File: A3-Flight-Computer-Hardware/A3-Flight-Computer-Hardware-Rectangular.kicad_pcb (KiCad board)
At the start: 4 copper layers, 70 x 40 mm, 68 parts, among them J1 BAT, J2 ST1W008S4ER1500, J3 USB_C_Receptacle_USB2.0_14P, J4 Debug Header, J5 Cam 1, J6 Cam 2, J8 Telem, J9 CAN, Q1 IRLML0030, SW1 BOOT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

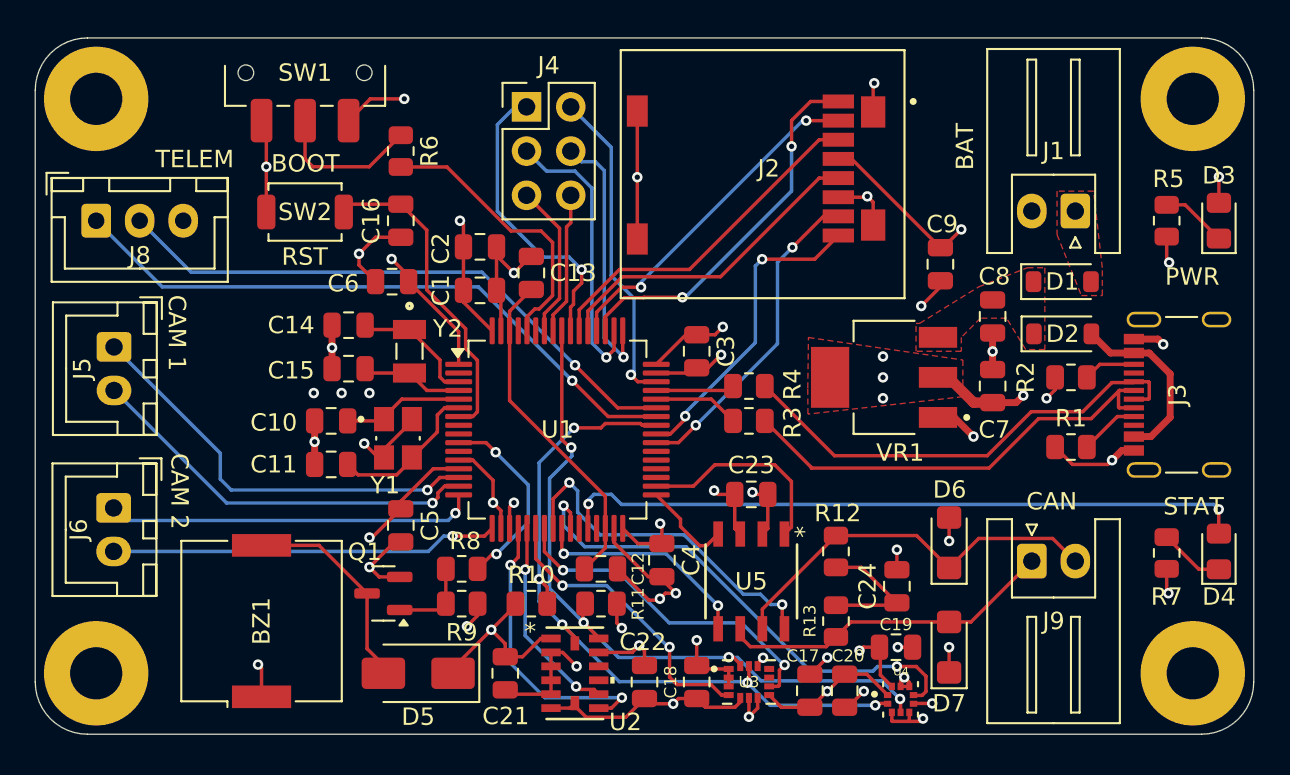
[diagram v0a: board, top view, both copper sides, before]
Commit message: Small routing changes
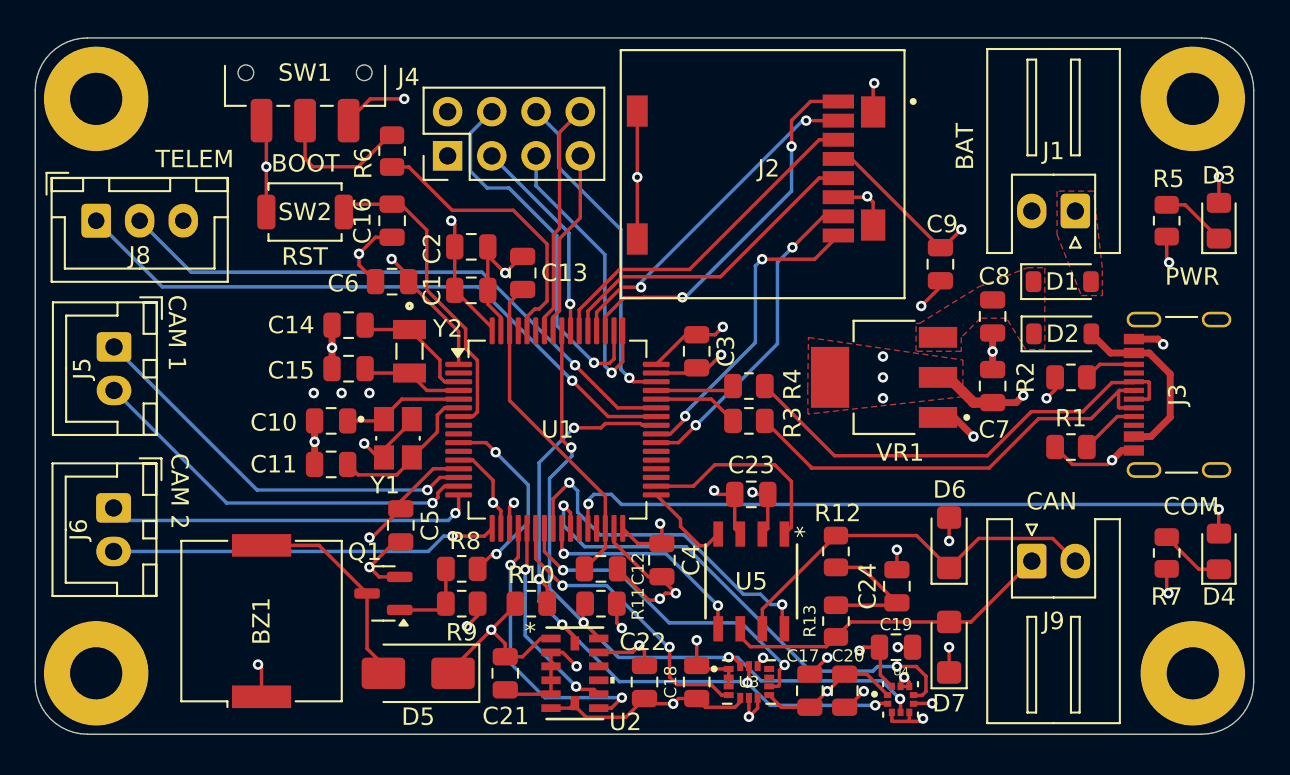
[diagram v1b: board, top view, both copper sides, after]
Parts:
- J4: value Debug Header -> Conn_02x04_Odd_Even; footprint Connector_PinHeader_2.54mm:PinHeader_2x03_P2.54mm_Vertical -> Connector_PinHeader_2.54mm:PinHeader_2x04_P2.54mm_Vertical
- moved J4 5.34 mm to (138.2, 88.3), turned to 90 degrees
- moved C1 0.50 mm to (139.6, 96.0)
- moved C13 0.50 mm to (142.5, 95.0)
- moved C16 0.50 mm to (135.0, 92.0)
- moved C2 0.50 mm to (139.6, 93.5)
- moved R6 0.50 mm to (135.0, 88.0)
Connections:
- J4 pad 1: /JTDO-SWO -> GND
- J4 pad 2: /JTMS-SWDIO -> +3.3V
- J4 pad 3: /JTDI -> /JTDO-SWO
- J4 pad 4: /JTCK-SWCLK -> /JTDI
- J4 pad 5: /DEBUG_RX -> /JTCK-SWCLK
- J4 pad 6: /DEBUG_TX -> /JTMS-SWDIO
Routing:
- net /JTDO-SWO: track 17.1 -> 11.9 mm
- net /JTDI: track 16.4 -> 21.5 mm
- net /DEBUG_RX: track 8.93 -> 13.4 mm
- net /DEBUG_TX: track 8.21 -> 10.7 mm
- net /JTCK-SWCLK: track 15.1 -> 16.9 mm
- net /CAM1_TX: track 24.4 -> 23.5 mm
- net /JTMS-SWDIO: track 18.6 -> 19.2 mm
- net /BOOT: track 16.3 -> 15.8 mm
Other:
- board text added: "COM"
- board text removed: "STAT"

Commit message: Added labels and changed component sizes
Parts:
- removed the D5 at (136.5, 118.0)
- added C7: 100nF, Capacitor_SMD:C_0402_1005Metric, F.Cu at (141.2, 111.2)
- added D4: LED, LED_SMD:LED_0805_2012Metric_Pad1.15x1.40mm_HandSolder, F.Cu at (179.0, 111.0)
- added D6: DSS14U, Diode_SMD:D_SOD-123, F.Cu at (134.5, 116.0)
- added R7: 240R, Resistor_SMD:R_0402_1005Metric, F.Cu at (179.0, 108.0)
- added TP3: SDA, TestPoint:TestPoint_THTPad_1.0x1.0mm_Drill0.5mm, F.Cu at (165.9, 118.0)
- added TP4: SCL, TestPoint:TestPoint_THTPad_1.0x1.0mm_Drill0.5mm, F.Cu at (162.9, 118.0)
- C10: renamed from C9; footprint Capacitor_SMD:C_0805_2012Metric -> Capacitor_SMD:C_0402_1005Metric
- C11: renamed from C10; footprint Capacitor_SMD:C_0805_2012Metric -> Capacitor_SMD:C_0402_1005Metric
- C12: renamed from C11; footprint Capacitor_SMD:C_0805_2012Metric -> Capacitor_SMD:C_0402_1005Metric
- C13: renamed from C12; footprint Capacitor_SMD:C_0805_2012Metric -> Capacitor_SMD:C_0402_1005Metric
- C14: renamed from C13; footprint Capacitor_SMD:C_0805_2012Metric -> Capacitor_SMD:C_0402_1005Metric
- C15: renamed from C14; footprint Capacitor_SMD:C_0805_2012Metric -> Capacitor_SMD:C_0402_1005Metric
- C16: renamed from C15; footprint Capacitor_SMD:C_0805_2012Metric -> Capacitor_SMD:C_0402_1005Metric
- C17: renamed from C16; footprint Capacitor_SMD:C_0805_2012Metric -> Capacitor_SMD:C_0402_1005Metric
- C18: renamed from C17; footprint Capacitor_SMD:C_0805_2012Metric -> Capacitor_SMD:C_0402_1005Metric
- C19: renamed from C18; footprint Capacitor_SMD:C_0805_2012Metric -> Capacitor_SMD:C_0402_1005Metric
- C2, C3, C4, C5, C6: footprint Capacitor_SMD:C_0805_2012Metric -> Capacitor_SMD:C_0402_1005Metric
- C20: renamed from C19; footprint Capacitor_SMD:C_0805_2012Metric -> Capacitor_SMD:C_0402_1005Metric
- C21: renamed from C20; footprint Capacitor_SMD:C_0805_2012Metric -> Capacitor_SMD:C_0402_1005Metric
- C22: renamed from C21; footprint Capacitor_SMD:C_0805_2012Metric -> Capacitor_SMD:C_0402_1005Metric
- C23: renamed from C22; footprint Capacitor_SMD:C_0805_2012Metric -> Capacitor_SMD:C_0402_1005Metric
- C24: renamed from C23; footprint Capacitor_SMD:C_0805_2012Metric -> Capacitor_SMD:C_0402_1005Metric
- C25: renamed from C24; footprint Capacitor_SMD:C_0805_2012Metric -> Capacitor_SMD:C_0402_1005Metric
- J4: renamed from J5; footprint Connector_JST:JST_XH_B2B-XH-A_1x02_P2.50mm_Vertical -> Connector_JST:JST_XH_S2B-XH-A_1x02_P2.50mm_Horizontal
- J5: renamed from J4; value Conn_02x04_Odd_Even -> DEBUG
- J6: footprint Connector_JST:JST_XH_B2B-XH-A_1x02_P2.50mm_Vertical -> Connector_JST:JST_XH_S2B-XH-A_1x02_P2.50mm_Horizontal
- J7: renamed from J8; footprint Connector_JST:JST_XH_B3B-XH-A_1x03_P2.50mm_Vertical -> Connector_JST:JST_XH_S3B-XH-A_1x03_P2.50mm_Horizontal
- R1, R2, R3, R4, R5, R6: footprint Resistor_SMD:R_0805_2012Metric -> Resistor_SMD:R_0402_1005Metric
- R10: renamed from R9; footprint Resistor_SMD:R_0805_2012Metric -> Resistor_SMD:R_0402_1005Metric
- R11: renamed from R10; footprint Resistor_SMD:R_0805_2012Metric -> Resistor_SMD:R_0402_1005Metric
- R12: renamed from R11; footprint Resistor_SMD:R_0805_2012Metric -> Resistor_SMD:R_0402_1005Metric
- R13: renamed from R12; footprint Resistor_SMD:R_0805_2012Metric -> Resistor_SMD:R_0402_1005Metric
- R14: renamed from R13; footprint Resistor_SMD:R_0805_2012Metric -> Resistor_SMD:R_0402_1005Metric
- R8: renamed from R7; footprint Resistor_SMD:R_0805_2012Metric -> Resistor_SMD:R_0402_1005Metric
- R9: renamed from R8; footprint Resistor_SMD:R_0805_2012Metric -> Resistor_SMD:R_0402_1005Metric
- moved J7 20.6 mm to (124.5, 111.6)
- moved C22 17.5 mm to (159.0, 117.0)
- moved BZ1 14.1 mm to (141.5, 116.5), turned to 180 degrees
- moved C19 12.3 mm to (163.5, 113.0), turned to -90 degrees
- moved U4 11.0 mm to (155.0, 113.5), turned to -90 degrees
- moved U2 10.0 mm to (155.5, 118.0), turned to -90 degrees
- moved C21 9.60 mm to (155.0, 111.5), turned to 180 degrees
- moved J4 8.46 mm to (124.4, 92.8)
- moved J6 8.29 mm to (124.4, 102.2)
- moved R11 8.25 mm to (151.0, 112.0), turned to -90 degrees
- moved C20 7.58 mm to (157.0, 113.5), turned to -90 degrees
- moved U3 6.87 mm to (161.1, 114.5), turned to 90 degrees
- moved D8 6.58 mm to (166.0, 110.0), turned to 0 degrees
- moved C18 6.02 mm to (163.5, 115.0)
- moved R14 5.63 mm to (161.7, 109.5)
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- renumbered C7 to C8, C8 to C9, D4 to D5, D6 to D7, D7 to D8, J9 to J8
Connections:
- net /STAT_LED renamed /STAT_LED2
- U1 pad 10: /BUZZ -> unconnected-(U1-PC2-Pad10)
- U1 pad 24: /CAN_STBD -> /BUZZ
- U1 pad 25: /CAN_SHD -> unconnected-(U1-PC5-Pad25)
- U1 pad 27: unconnected-(U1-PB1-Pad27) -> /STAT_LED1
- U1 pad 35: unconnected-(U1-PB14-Pad35) -> /CAN_SHD
- U1 pad 36: unconnected-(U1-PB15-Pad36) -> /CAN_STBD
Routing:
- net +3.3V: track 96.3 -> 50.7 mm, vias 22 -> 24
- net /STAT_LED1: track 0.00 -> 36.2 mm, vias 0 -> 2
- net GND: track 116.4 -> 82.3 mm, vias 36 -> 49
- net /LPS22HB_INT: track 28.9 -> 13.8 mm
- net /CAM1_RX: track 23.0 -> 36.1 mm
- net /CAN_STBD: track 20.3 -> 10.7 mm, vias 2 -> 0
- net /I2C_SDA: track 42.6 -> 50.1 mm, vias 4 -> 3
- net /FDCAN_TX: track 11.9 -> 4.80 mm
- net /LSM6_INT1: track 17.2 -> 23.4 mm, vias 2 -> 0
- net /ADXL375_INT2: track 11.8 -> 17.8 mm, vias 2 -> 0
- net Net-(D8-A2): track 19.5 -> 13.8 mm
- net Net-(SW1-B): track 8.64 -> 2.99 mm
- net /TELEM_RX: track 34.1 -> 28.8 mm
- net Net-(D7-A1): track 22.9 -> 18.0 mm
- net /TELEM_TX: track 36.8 -> 32.3 mm
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- added copper zone on F.Cu, net GND
- added copper zone on F.Cu, net Net-(D2-A)
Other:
- board text added: "3V3"
- board text added: "CANH"
- board text added: "CANL"
- board text added: "GND"
- board text added: "JTCK SWCLK"
- board text added: "JTDI"
- board text added: "JTDO SWO"
- board text added: "JTMS SWDIO"
- board text added: "RX"
- board text added: "TX"

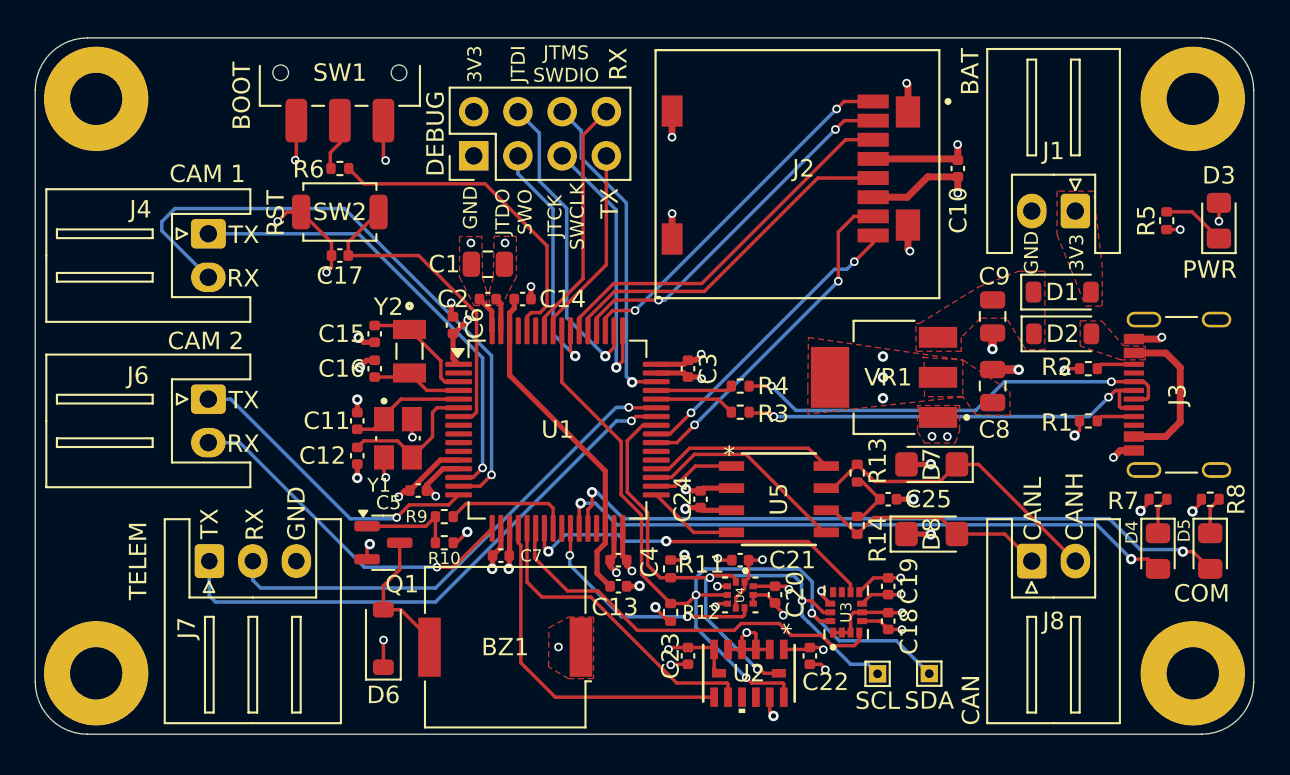
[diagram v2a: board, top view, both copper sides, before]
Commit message: Updated gerber files + BOM for purchasing
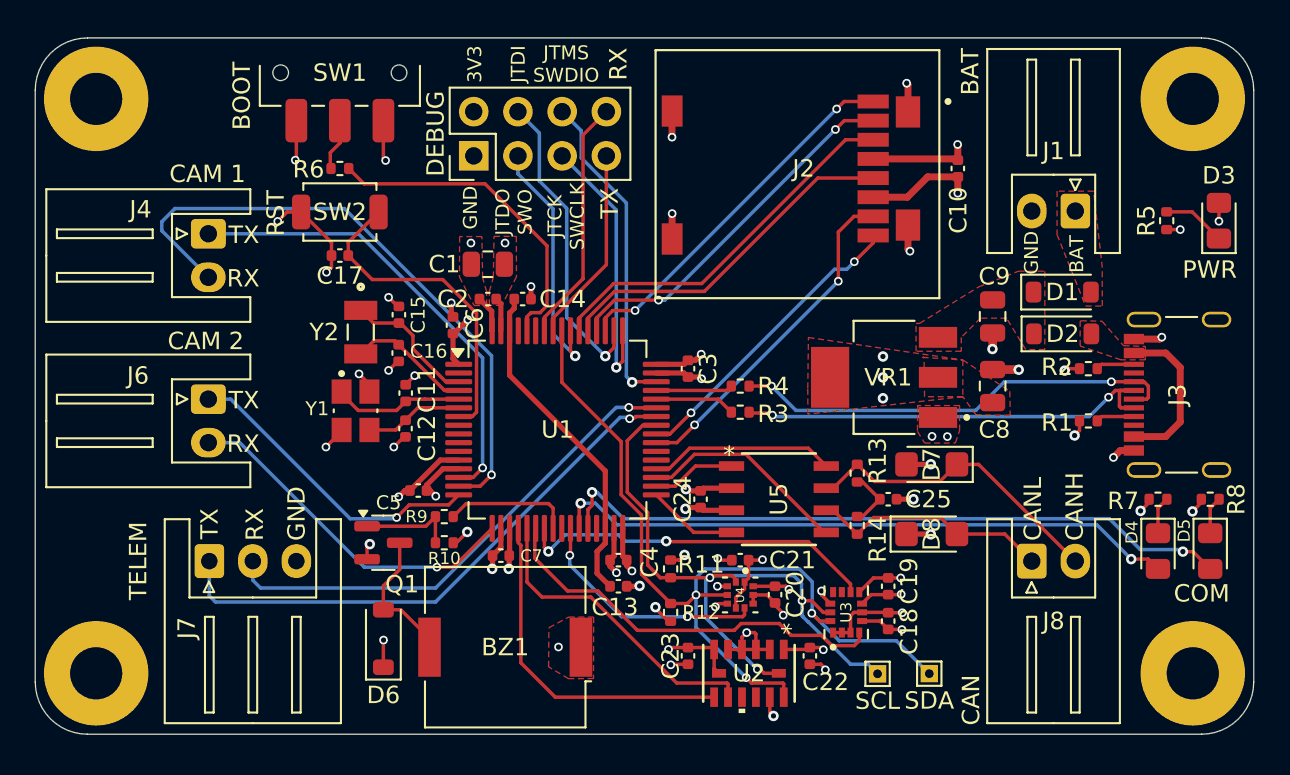
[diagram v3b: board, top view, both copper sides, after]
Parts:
- moved C11 3.21 mm to (135.8, 101.9)
- moved C12 3.18 mm to (135.8, 103.9)
- moved Y2 3.01 mm to (133.2, 98.4)
- moved Y1 2.90 mm to (132.9, 102.9)
- moved C15 1.77 mm to (135.4, 97.4), turned to 90 degrees
- moved C16 1.65 mm to (135.4, 99.6), turned to -90 degrees
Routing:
- net /HSE_OUT: track 8.45 -> 5.65 mm
- net /LSE_OUT: track 5.33 -> 7.12 mm
- net /LSE_IN: track 6.73 -> 7.77 mm
- net /HSE_IN: track 6.65 -> 7.51 mm
